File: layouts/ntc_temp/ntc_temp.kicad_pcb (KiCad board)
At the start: 2 copper layers, 2 parts

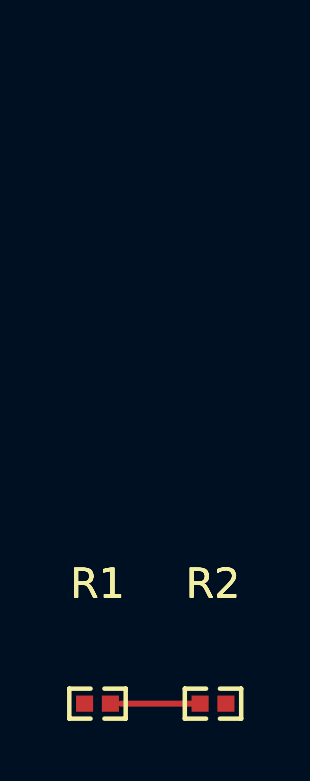
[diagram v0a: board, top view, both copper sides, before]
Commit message: Enhance smart placer with simulated annealing and pre-routing validation
Smart Placer improvements:
- Add simulated annealing refinement (now default) for better wire length optimization
- Add force-directed refinement with improvement safeguard
- Add silkscreen text repositioning to avoid component overlaps
- Significant wire length reductions (e.g., power_filter: 113mm -> 46mm)

Autorouter improvements:
- Add PreRoutingValidator class for pre-flight checks
- Validate unconnected pads, overlapping footprints, unplaced components
- Use pad-based bounds for accurate overlap detection
- Block routing on validation errors with actionable messages

Research:
- Add comprehensive autorouting/autoplacement findings document
- Cover Freerouting Python client, OrthoRoute, DeepPCB, KiCad 9 IPC API
- Document force-directed and simulated annealing algorithms

Cleanup:
- Update .gitignore for DSN/SES files, build artifacts, tools
- Remove stale timestamped build files
- Add parts footprints and symbols

All 10 modules placed and routed successfully.

Co-Authored-By: Claude Opus 4.5 <noreply@anthropic.com>
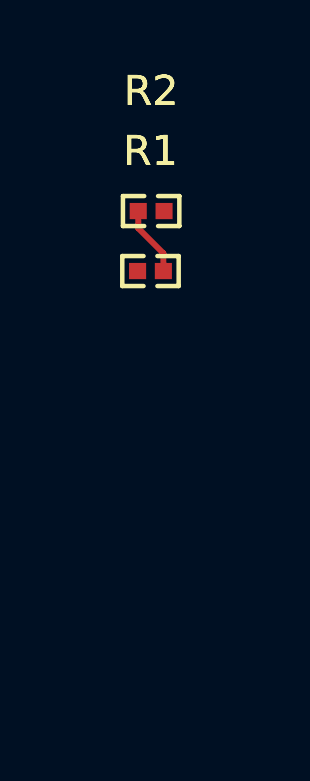
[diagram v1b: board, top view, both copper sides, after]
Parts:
- moved R2 16.5 mm to (97.9, 83.6)
- moved R1 14.5 mm to (97.9, 85.6)
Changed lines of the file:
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@@
 	(footprint "Murata_Electronics_NCP15XH103F03RC:R0402"
 		(layer "F.Cu")
-		(at 100 100)
+		(at 97.9381 83.5799)
 		(property "Reference" "R2"
 			(at 0 -4 0)
@@
 	(footprint "UNI_ROYAL_0402WGF1002TCE:R0402"
 		(layer "F.Cu")
-		(at 96.15 100)
+		(at 97.916 85.5795)
 		(property "Reference" "R1"
 			(at 0 -4 0)
@@
 	)
 	(segment
-		(start 99.57 100)
-		(end 96.93 100)
+		(start 97.5081 84.1516)
+		(end 98.346 84.9895)
 		(width 0.2)
 		(layer "F.Cu")
+		(net 1)
+	)
+	(segment
+		(start 98.346 84.9895)
+		(end 98.346 85.5795)
+		(width 0.2)
+		(layer "F.Cu")
+		(net 1)
+	)
+	(segment
+		(start 97.5081 83.5799)
+		(end 97.5081 84.1516)
+		(width 0.2)
+		(layer "F.Cu")
